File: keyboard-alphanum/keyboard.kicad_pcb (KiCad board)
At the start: 2 copper layers, 76.2 x 113.8 mm, 80 parts, among them J1 Prog pings, J3 ST-Link, J4 USB_B_Mini, J5 USB_A, J6 USB_A, J7 USB_A, J8 UART, SW1 NL, SW10 plus, SW11 2, SW12 sub, SW13 4, SW14 3, SW15 7, SW16 5, SW17 enter, SW2 8, SW3 6, SW4 0, SW5 div, SW6 9, SW7 1, SW8 dot, SW9 mul, U1 STM32F103C6T6A, U2 LD1117S33TR, U3 HS8836A, Y1 8MHz, Y3 32768MHz

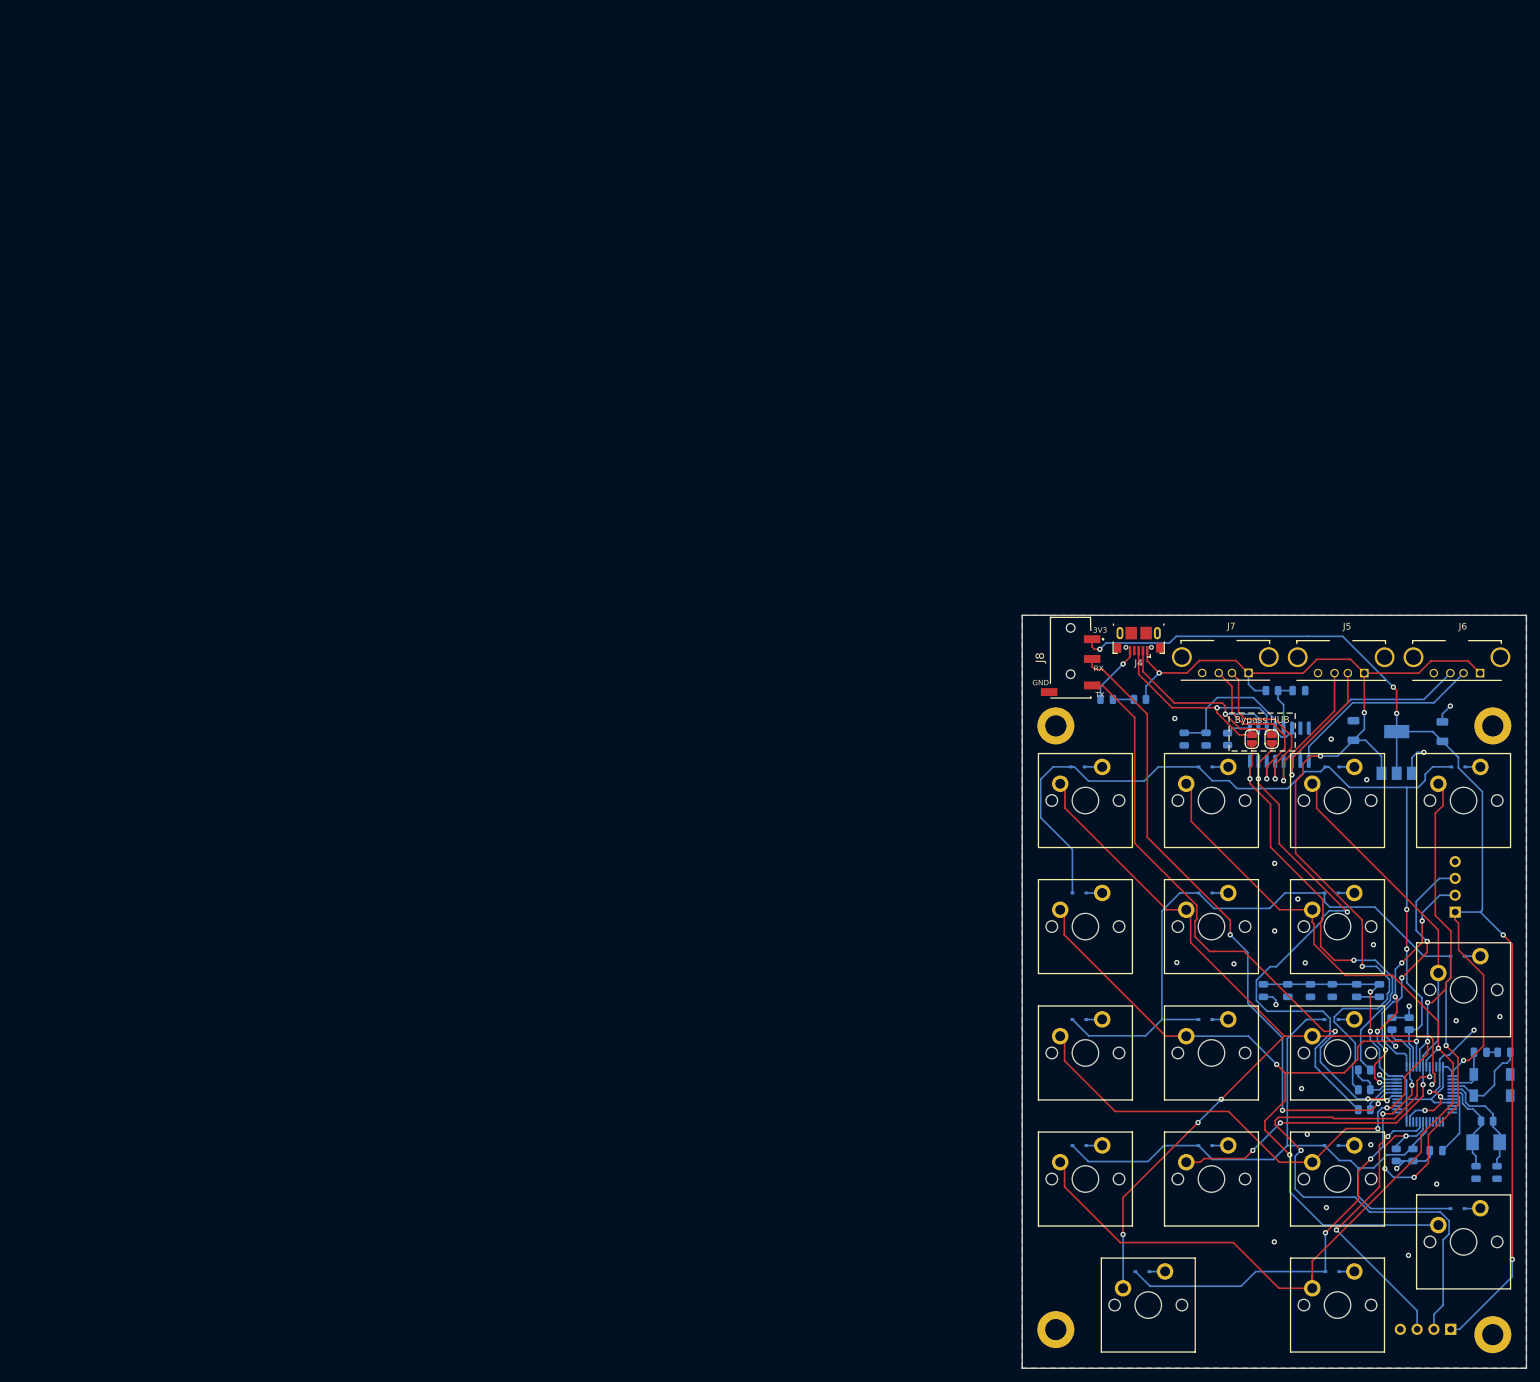
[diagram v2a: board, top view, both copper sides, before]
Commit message: Update latest version of keyboard-personal
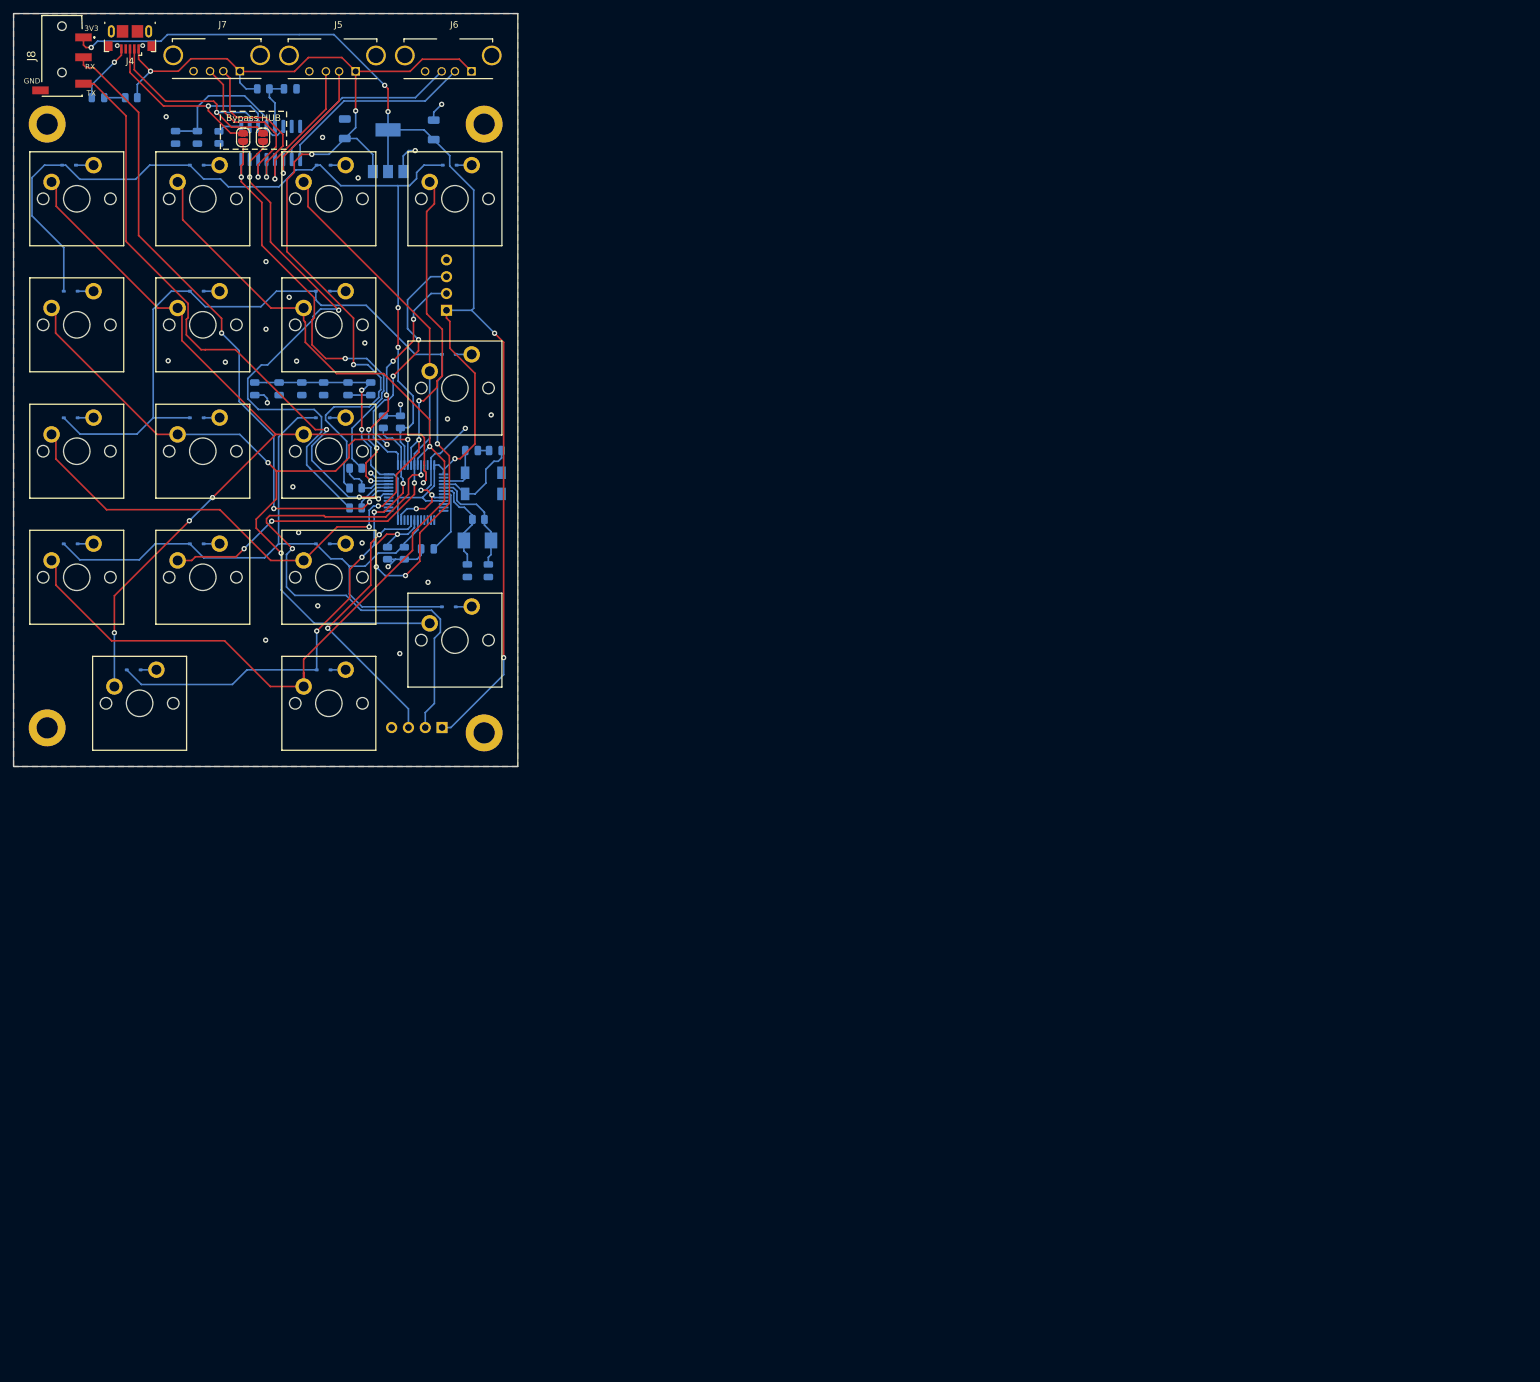
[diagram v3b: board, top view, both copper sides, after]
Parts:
- moved C1 177.5 mm to (30.4, 27.5)
- moved C11 177.5 mm to (-1.69, 0.06)
- moved C12 177.5 mm to (25.4, -39.1)
- moved C13 177.5 mm to (11.9, -39.2)
- moved C14 177.5 mm to (-10.4, -37.9)
- moved C15 177.5 mm to (-13.7, -37.9)
- moved C16 177.5 mm to (3.68, -45.3)
- moved C2 177.5 mm to (33.6, 27.5)
- moved C3 177.5 mm to (34.7, 9.39)
- moved C5 177.5 mm to (24.4, 24.2)
- moved C6 177.5 mm to (15.8, 0.06)
- moved C7 177.5 mm to (12.4, 0.06)
- moved C8 177.5 mm to (8.72, 0.06)
- moved D1 177.5 mm to (-29.8, -33.7)
- moved D10 177.5 mm to (27.6, -5.14)
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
